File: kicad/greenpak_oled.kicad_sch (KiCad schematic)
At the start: 21 parts, among them J1 Conn_01x05_Pin, J2 Conn_01x03_Socket, U1 SLG46826G, U2 OLED-128O064D

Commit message: Renamed left over addressable_oled to greenpak_oled.
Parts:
- C1, C2, C3, C4, C5, C6, C7, C8, C9: footprint addressable_oled:C_0603_1608Metric -> greenpak_oled:C_0603_1608Metric
- H1, H2, H3, H4: footprint addressable_oled:MountingHole -> greenpak_oled:MountingHole
- J1: footprint addressable_oled:PinHeader_1x05_P2.54mm_Vertical -> greenpak_oled:PinHeader_1x05_P2.54mm_Vertical
- J2: footprint addressable_oled:PinHeader_1x04_P2.54mm_Vertical -> greenpak_oled:PinHeader_1x04_P2.54mm_Vertical
- JP1, JP2, JP4: footprint addressable_oled:SolderJumper-2_P1.3mm_Open_Pad1.0x1.5mm -> greenpak_oled:SolderJumper-2_P1.3mm_Open_Pad1.0x1.5mm; symbol addressable_oled:Jumper_2_Open -> greenpak_oled:Jumper_2_Open
- R3: footprint addressable_oled:R_0603_1608Metric -> greenpak_oled:R_0603_1608Metric
- U1: footprint addressable_oled:TSSOP20_MO-220_WECE_REN -> greenpak_oled:TSSOP20_MO-220_WECE_REN; symbol addressable_oled:SLG46826G -> greenpak_oled:SLG46826G
- U2: footprint addressable_oled:OLED-128O064D -> greenpak_oled:OLED-128O064D; symbol addressable_oled:OLED-128O064D -> greenpak_oled:OLED-128O064D

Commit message: Final touched. Regenerated gerbers.
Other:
- title: ADDRESSABLE SPI OLED -> GREENPAK OLED
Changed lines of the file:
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@@
   (paper "USLetter")
   (title_block
-    (title "ADDRESSABLE SPI OLED")
+    (title "GREENPAK OLED")
     (rev "0.1")
   )

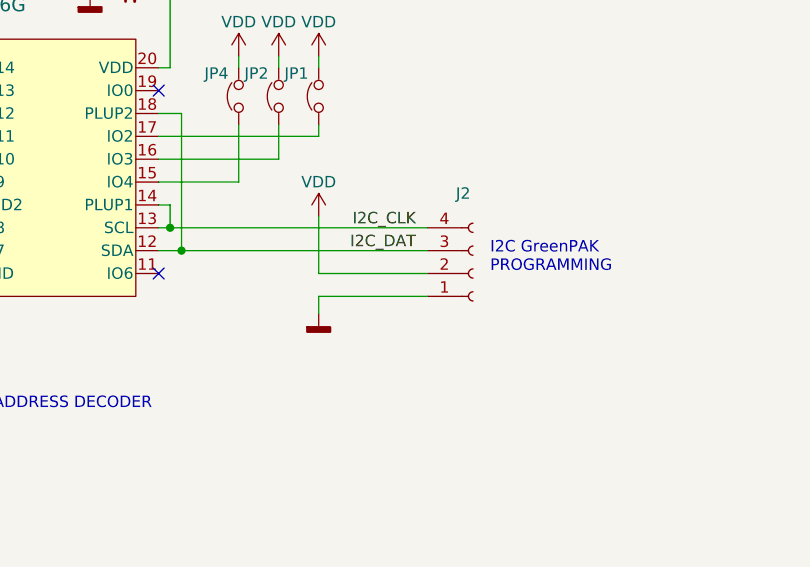
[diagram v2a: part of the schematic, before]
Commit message: Changed programming pads to pogo socket.
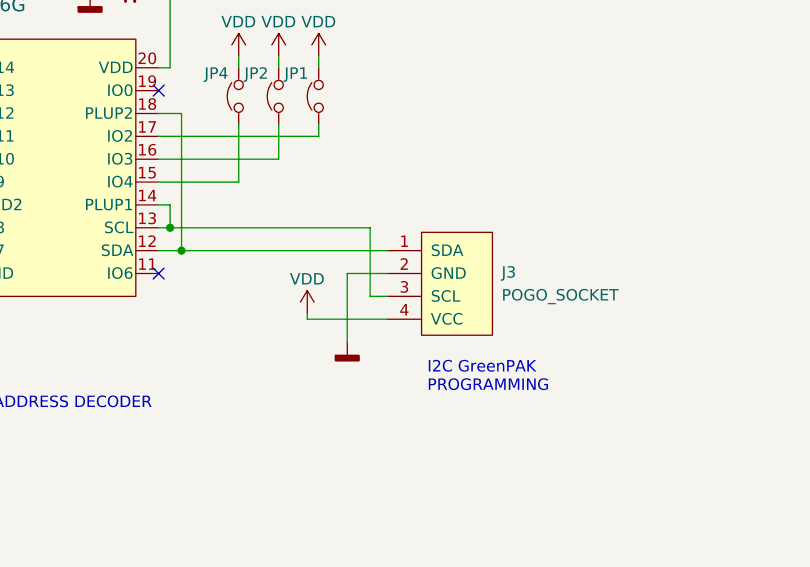
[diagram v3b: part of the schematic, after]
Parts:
- removed J2: Conn_01x03_Socket, greenpak_oled:PinHeader_1x04_P2.54mm_Vertical, symbol Connector:Conn_01x04_Socket
- added J3: POGO_SOCKET, greenpak_oled:POGO_SOCKET, symbol greenpak_oled:POGO_SOCKET
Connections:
- net GND: now also J3.2 (GND)
- net VDD: now also J3.4 (VCC)
- net I2C_CLK: no longer names the net of U1.13 (SCL), U1.14 (PLUP1)
- net I2C_CLK: now also J3.3 (SCL)
- net I2C_DAT: no longer names the net of U1.12 (SDA), U1.18 (PLUP2)
- net I2C_DAT: now also J3.1 (SDA)
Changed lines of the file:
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@@
   (title_block
     (title "GREENPAK OLED")
-    (rev "0.1")
+    (rev "0.2")
   )
   (junction (at 185.42 113.03) (diameter 0) (color 0 0 0 0)
@@
     (stroke (width 0) (type default))
   )
-  (wire (pts (xy 127 137.795) (xy 114.935 137.795))
-    (stroke (width 0) (type default))
-  )
   (wire (pts (xy 97.155 130.175) (xy 98.425 130.175))
     (stroke (width 0) (type default))
@@
     (stroke (width 0) (type default))
   )
-  (wire (pts (xy 114.935 140.335) (xy 114.935 142.24))
+  (wire (pts (xy 118.11 137.795) (xy 118.11 145.415))
     (stroke (width 0) (type default))
   )
@@
     (stroke (width 0) (type default))
   )
-  (wire (pts (xy 114.935 131.445) (xy 114.935 137.795))
-    (stroke (width 0) (type default))
-  )
   (wire (pts (xy 62.23 117.475) (xy 74.295 117.475))
     (stroke (width 0) (type default))
@@
     (stroke (width 0) (type default))
   )
+  (wire (pts (xy 120.65 140.335) (xy 122.555 140.335))
+    (stroke (width 0) (type default))
+  )
   (wire (pts (xy 97.155 122.555) (xy 114.935 122.555))
     (stroke (width 0) (type default))
@@
     (stroke (width 0) (type default))
   )
+  (wire (pts (xy 120.65 132.715) (xy 120.65 140.335))
+    (stroke (width 0) (type default))
+  )
   (wire (pts (xy 97.155 114.935) (xy 98.425 114.935))
     (stroke (width 0) (type default))
@@
     (stroke (width 0) (type default))
   )
+  (wire (pts (xy 113.665 142.875) (xy 113.665 142.24))
+    (stroke (width 0) (type default))
+  )
   (wire (pts (xy 210.185 55.245) (xy 207.01 55.245))
     (stroke (width 0) (type default))
@@
     (stroke (width 0) (type default))
   )
-  (wire (pts (xy 98.425 132.715) (xy 127 132.715))
+  (wire (pts (xy 98.425 132.715) (xy 120.65 132.715))
     (stroke (width 0) (type default))
   )
@@
     (stroke (width 0) (type default))
   )
-  (wire (pts (xy 99.695 135.255) (xy 127 135.255))
+  (wire (pts (xy 99.695 135.255) (xy 122.555 135.255))
     (stroke (width 0) (type default))
   )
@@
     (stroke (width 0) (type default))
   )
+  (wire (pts (xy 122.555 142.875) (xy 113.665 142.875))
+    (stroke (width 0) (type default))
+  )
   (wire (pts (xy 197.485 139.7) (xy 200.66 139.7))
     (stroke (width 0) (type default))
@@
     (stroke (width 0) (type default))
   )
-  (wire (pts (xy 127 140.335) (xy 114.935 140.335))
+  (wire (pts (xy 122.555 137.795) (xy 118.11 137.795))
     (stroke (width 0) (type default))
   )
@@
     (effects (font (size 1.27 1.27)) (justify left bottom))
   )
-  (text "I2C GreenPAK\nPROGRAMMING" (at 133.985 137.795 0)
+  (text "I2C GreenPAK\nPROGRAMMING" (at 127 151.13 0)
     (effects (font (size 1.27 1.27)) (justify left bottom))
   )
@@
     (effects (font (size 1.27 1.27)) (justify left bottom))
   )
-  (label "I2C_CLK" (at 125.73 132.715 180) (fields_autoplaced)
-    (effects (font (size 1.27 1.27)) (justify right bottom))
-  )
   (label "OLED_DC" (at 172.085 95.25 0) (fields_autoplaced)
     (effects (font (size 1.27 1.27)) (justify left bottom))
@@
   (label "OLED_CS" (at 62.23 122.555 0) (fields_autoplaced)
     (effects (font (size 1.27 1.27)) (justify left bottom))
-  )
-  (label "I2C_DAT" (at 125.73 135.255 180) (fields_autoplaced)
-    (effects (font (size 1.27 1.27)) (justify right bottom))
   )
   (symbol (lib_id "greenpak_oled:Jumper_2_Open") (at 110.49 118.11 90) (unit 1)
@@
     )
   )
-  (symbol (lib_id "greenpak_oled:GND") (at 114.935 142.24 0) (unit 1)
+  (symbol (lib_id "greenpak_oled:GND") (at 118.11 145.415 0) (unit 1)
     (in_bom yes) (on_board yes) (dnp no) (fields_autoplaced)
-    (property "Reference" "#PWR011" (at 114.935 148.59 0)
-      (effects (font (size 1.27 1.27)) hide)
-    )
-    (property "Value" "GND" (at 114.935 147.32 0)
-      (effects (font (size 1.27 1.27)) hide)
-    )
-    (property "Footprint" "" (at 114.935 142.24 0)
-      (effects (font (size 1.27 1.27)) hide)
-    )
-    (property "Datasheet" "" (at 114.935 142.24 0)
+    (property "Reference" "#PWR011" (at 118.11 151.765 0)
+      (effects (font (size 1.27 1.27)) hide)
+    )
+    (property "Value" "GND" (at 118.11 150.495 0)
+      (effects (font (size 1.27 1.27)) hide)
+    )
+    (property "Footprint" "" (at 118.11 145.415 0)
+      (effects (font (size 1.27 1.27)) hide)
+    )
+    (property "Datasheet" "" (at 118.11 145.415 0)
       (effects (font (size 1.27 1.27)) hide)
     )
@@
     )
   )
-  (symbol (lib_id "power:VDD") (at 114.935 131.445 0) (unit 1)
-    (in_bom yes) (on_board yes) (dnp no)
-    (property "Reference" "#PWR012" (at 114.935 135.255 0)
-      (effects (font (size 1.27 1.27)) hide)
-    )
-    (property "Value" "VDD" (at 114.935 127.635 0)
-      (effects (font (size 1.27 1.27)))
-    )
-    (property "Footprint" "" (at 114.935 131.445 0)
-      (effects (font (size 1.27 1.27)) hide)
-    )
-    (property "Datasheet" "" (at 114.935 131.445 0)
+  (symbol (lib_id "power:VDD") (at 113.665 142.24 0) (unit 1)
+    (in_bom yes) (on_board yes) (dnp no)
+    (property "Reference" "#PWR012" (at 113.665 146.05 0)
+      (effects (font (size 1.27 1.27)) hide)
+    )
+    (property "Value" "VDD" (at 113.665 138.43 0)
+      (effects (font (size 1.27 1.27)))
+    )
+    (property "Footprint" "" (at 113.665 142.24 0)
+      (effects (font (size 1.27 1.27)) hide)
+    )
+    (property "Datasheet" "" (at 113.665 142.24 0)
       (effects (font (size 1.27 1.27)) hide)
     )
@@
         (path "/7b608d4d-4c17-4227-91f9-c343a36b0392"
           (reference "#PWR020") (unit 1)
+        )
+      )
+    )
+  )
+  (symbol (lib_id "greenpak_oled:POGO_SOCKET") (at 131.445 139.7 0) (unit 1)
+    (in_bom yes) (on_board yes) (dnp no) (fields_autoplaced)
+    (property "Reference" "J3" (at 135.255 137.668 0)
+      (effects (font (size 1.27 1.27)) (justify left))
+    )
+    (property "Value" "POGO_SOCKET" (at 135.255 140.208 0)
+      (effects (font (size 1.27 1.27)) (justify left))
+    )
+    (property "Footprint" "greenpak_oled:POGO_SOCKET" (at 128.524 151.892 0)
+      (effects (font (size 1.27 1.27)) hide)
+    )
+    (property "Datasheet" "~" (at 130.429 130.937 0) (do_not_autoplace)
+      (effects (font (size 1.27 1.27)) hide)
+    )
+    (pin "1")
+    (pin "4")
+    (pin "3")
+    (pin "2")
+    (instances
+      (project "greenpak_oled"
+        (path "/7b608d4d-4c17-4227-91f9-c343a36b0392"
+          (reference "J3") (unit 1)
         )
       )
@@
         )
       )
-    )
-  )
-  (symbol (lib_id "Connector:Conn_01x04_Socket") (at 132.08 137.795 0) (mirror x) (unit 1)
-    (in_bom yes) (on_board yes) (dnp no)
-    (property "Reference" "J2" (at 130.175 128.905 0)
-      (effects (font (size 1.27 1.27)) (justify left))
-    )
-    (property "Value" "Conn_01x03_Socket" (at 133.985 135.89 0)
-      (effects (font (size 1.27 1.27)) (justify left) hide)
-    )
-    (property "Footprint" "greenpak_oled:PinHeader_1x04_P2.54mm_Vertical" (at 132.08 137.795 0)
-      (effects (font (size 1.27 1.27)) hide)
-    )
-    (property "Datasheet" "~" (at 132.08 137.795 0)
-      (effects (font (size 1.27 1.27)) hide)
-    )
-    (pin "1")
-    (pin "2")
-    (pin "3")
-    (pin "4")
-    (instances
-      (project "greenpak_oled"
-        (path "/7b608d4d-4c17-4227-91f9-c343a36b0392"
-          (reference "J2") (unit 1)
-        )
-      )

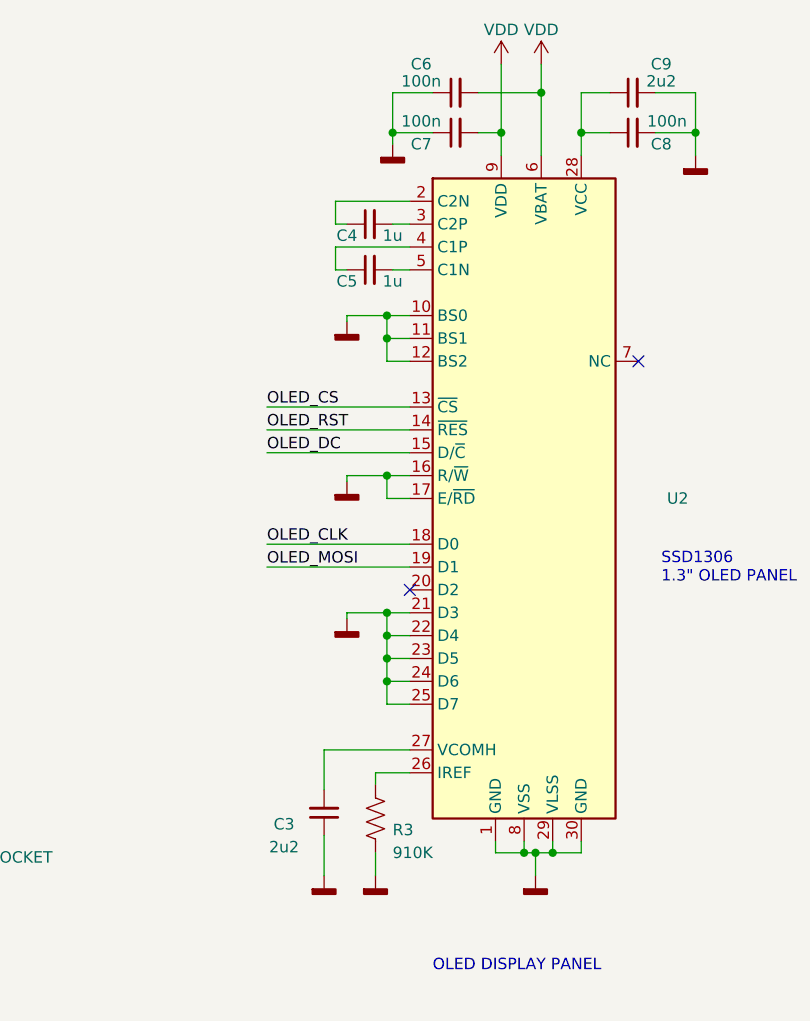
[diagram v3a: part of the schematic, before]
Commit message: Tweaked the schematic to match also SH1106.
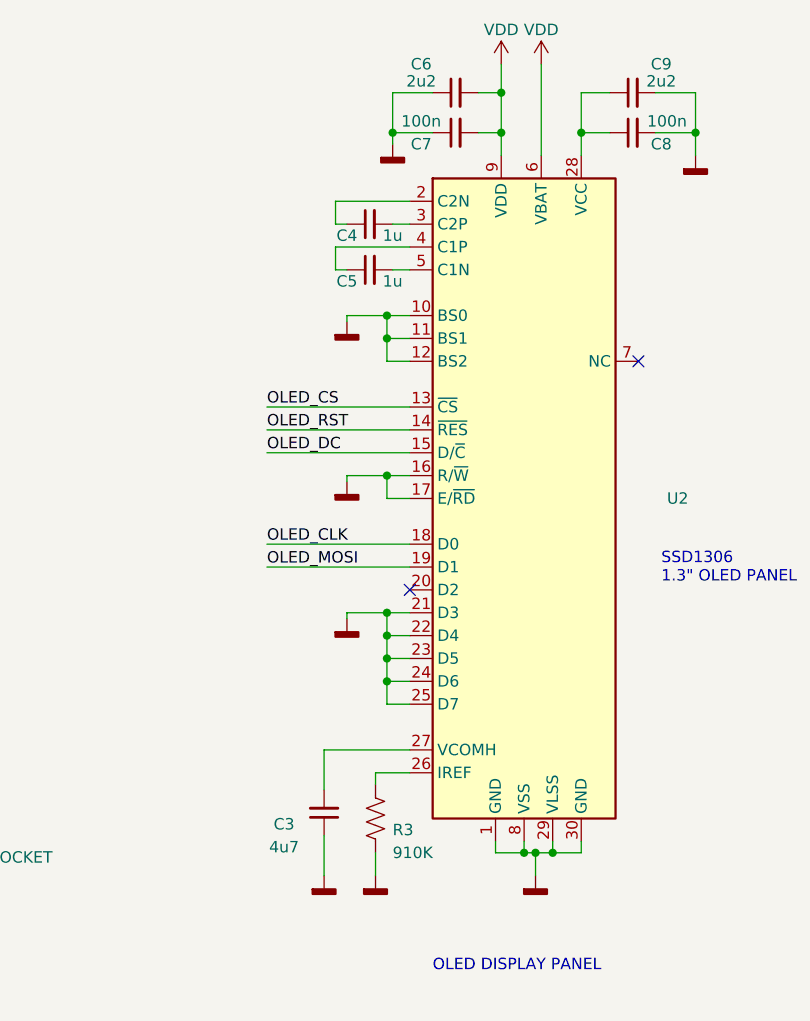
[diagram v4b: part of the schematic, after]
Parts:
- C3: value 2u2 -> 4u7
- C6: value 100n -> 2u2
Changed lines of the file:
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@@
   (junction (at 219.71 59.69) (diameter 0) (color 0 0 0 0)
   )
+  (junction (at 198.12 55.245) (diameter 0) (color 0 0 0 0)
+  )
   (junction (at 185.42 82.55) (diameter 0) (color 0 0 0 0)
   )
@@
   )
   (junction (at 185.42 115.57) (diameter 0) (color 0 0 0 0)
-  )
-  (junction (at 202.565 55.245) (diameter 0) (color 0 0 0 0)
   )
   (junction (at 98.425 106.045) (diameter 0) (color 0 0 0 0)
@@
     (stroke (width 0) (type default))
   )
-  (wire (pts (xy 202.565 55.245) (xy 202.565 62.23))
+  (wire (pts (xy 202.565 52.07) (xy 202.565 62.23))
     (stroke (width 0) (type default))
   )
@@
     (stroke (width 0) (type default))
   )
-  (wire (pts (xy 202.565 52.07) (xy 202.565 55.245))
-    (stroke (width 0) (type default))
-  )
   (wire (pts (xy 120.65 140.335) (xy 122.555 140.335))
     (stroke (width 0) (type default))
@@
     (stroke (width 0) (type default))
   )
+  (wire (pts (xy 195.58 55.245) (xy 198.12 55.245))
+    (stroke (width 0) (type default))
+  )
   (wire (pts (xy 62.23 114.935) (xy 74.295 114.935))
     (stroke (width 0) (type default))
@@
     (stroke (width 0) (type default))
   )
-  (wire (pts (xy 198.12 52.07) (xy 198.12 59.69))
+  (wire (pts (xy 198.12 52.07) (xy 198.12 55.245))
     (stroke (width 0) (type default))
   )
@@
     (stroke (width 0) (type default))
   )
-  (wire (pts (xy 195.58 55.245) (xy 202.565 55.245))
-    (stroke (width 0) (type default))
-  )
   (wire (pts (xy 74.295 130.175) (xy 53.975 130.175))
     (stroke (width 0) (type default))
@@
   )
   (wire (pts (xy 187.96 100.33) (xy 185.42 100.33))
+    (stroke (width 0) (type default))
+  )
+  (wire (pts (xy 198.12 55.245) (xy 198.12 59.69))
     (stroke (width 0) (type default))
   )
@@
       (effects (font (size 1.27 1.27)))
     )
-    (property "Value" "2u2" (at 173.99 139.065 0)
+    (property "Value" "4u7" (at 173.99 139.065 0)
       (effects (font (size 1.27 1.27)))
     )
@@
       (effects (font (size 1.27 1.27)))
     )
-    (property "Value" "100n" (at 189.23 53.975 90)
-      (effects (font (size 1.27 1.27)))
-    )
+    (property "Value" "2u2" (at 189.23 53.975 90)
+      (effects (font (size 1.27 1.27)))
+    )

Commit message: Updated pogo socket dimensions.
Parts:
- J3: footprint greenpak_oled:POGO_SOCKET -> greenpak_oled:GREENPAK_POGO_SOCKET
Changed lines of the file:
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@@
       (effects (font (size 1.27 1.27)) (justify left))
     )
-    (property "Footprint" "greenpak_oled:POGO_SOCKET" (at 128.524 151.892 0)
+    (property "Footprint" "greenpak_oled:GREENPAK_POGO_SOCKET" (at 128.524 151.892 0)
       (effects (font (size 1.27 1.27)) hide)
     )
